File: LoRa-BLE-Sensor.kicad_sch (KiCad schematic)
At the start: 123 parts, among them J1 SHF-105-01-X-D-SM, J10 Battery_with_NTC, J2 Conn_01x02_Socket, J3 Battery_Cell, J4 Conn_01x06_Socket, J5 Screw_Terminal_01x06, J6 Screw_Terminal_01x06, J7 Screw_Terminal_01x04, J8 Conn_01x04_Pin, J9 Conn_01x04_Pin, Q1 DMN67D7L, Q10 SQ2389ES, Q11 SQ2389ES, Q12 DMN62D0UDW-7, Q13 DMN62D0UDW-7, Q2 DMN67D7L, Q3 DMN67D7L, Q4 DMN67D7L, Q5 DMN67D7L, Q6 DMN67D7L, Q7 DMN67D7L, Q8 DMN67D7L, Q9 SQ2389ES, SW1 SW_Push, SW2 SW_Push, SW3 SW_Push, U1 RAK4630, U2 NPM1300-QEAA-R, U3 TLV61046ADBVR, U4 TLV61046ADBVR, U5 TLV61046ADBVR

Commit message: rearranged board down to 60mm
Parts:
- J3: footprint User_Connectors:18650_CLIP_PROTECTED -> Connector_JST:JST_PH_B2B-PH-SM4-TB_1x02-1MP_P2.00mm_Vertical
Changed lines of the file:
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@@
 			)
 		)
-		(property "Footprint" "User_Connectors:18650_CLIP_PROTECTED"
+		(property "Footprint" "Connector_JST:JST_PH_B2B-PH-SM4-TB_1x02-1MP_P2.00mm_Vertical"
 			(at 196.85 22.606 90)
 			(effects

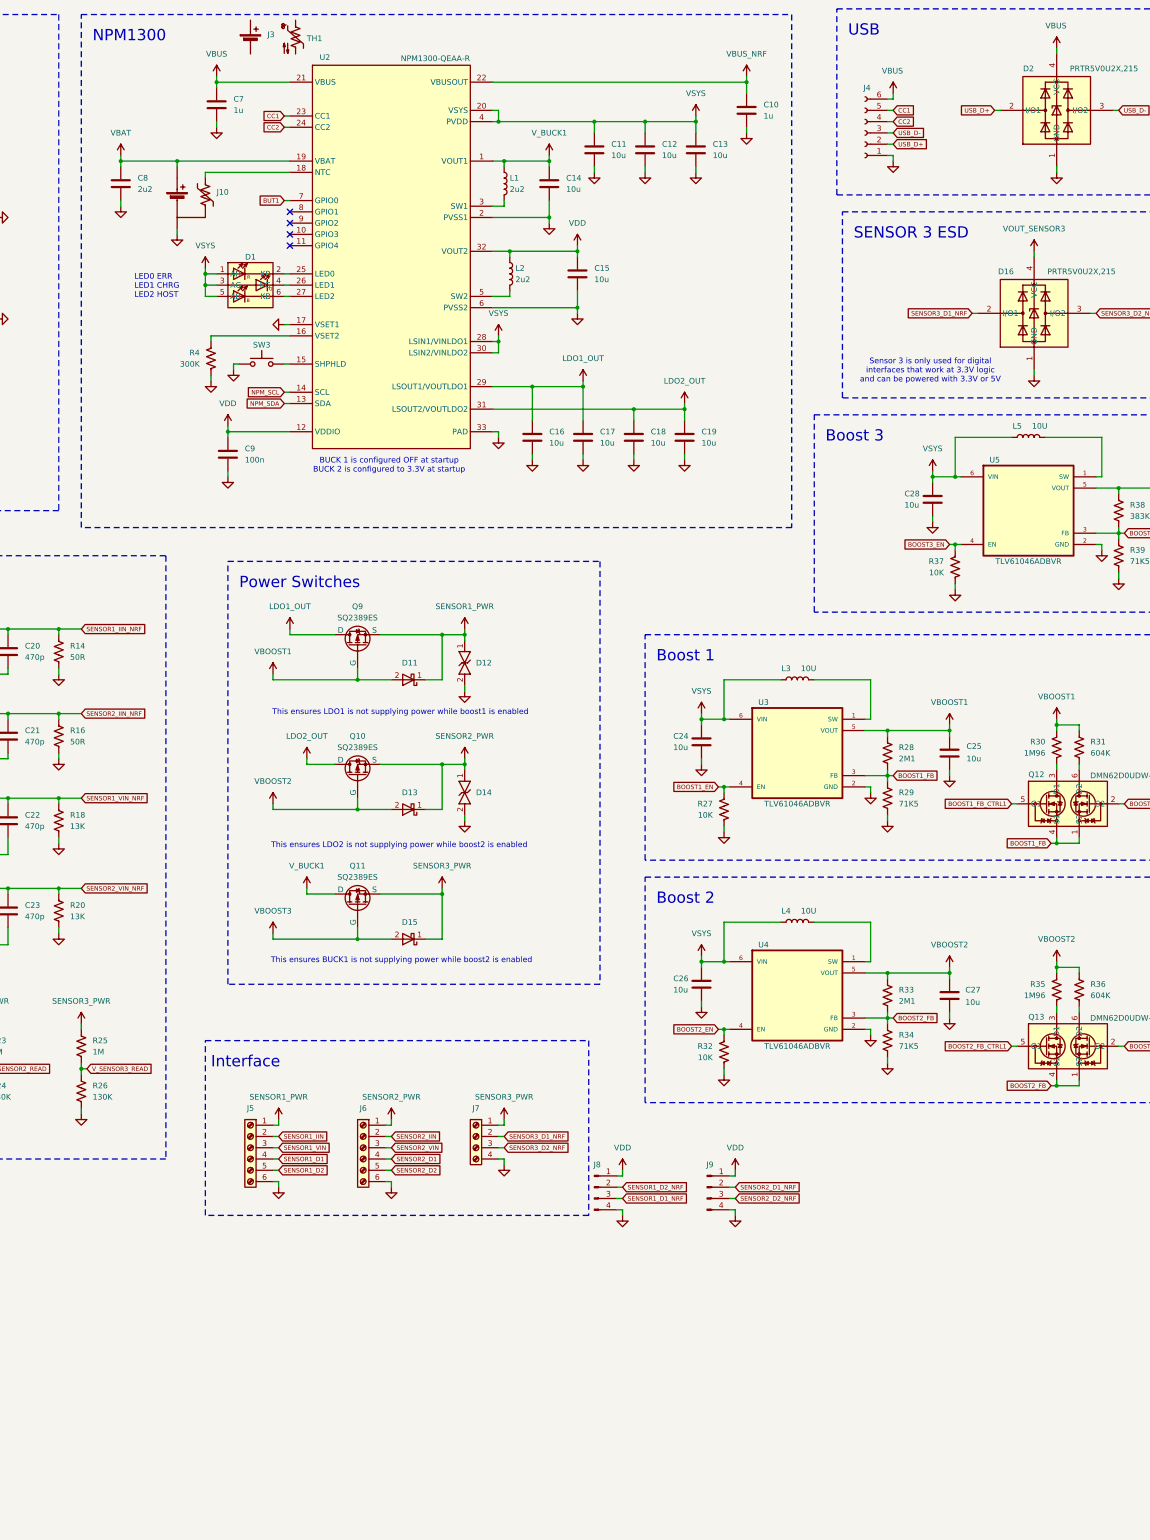
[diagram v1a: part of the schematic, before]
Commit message: external battery design finished
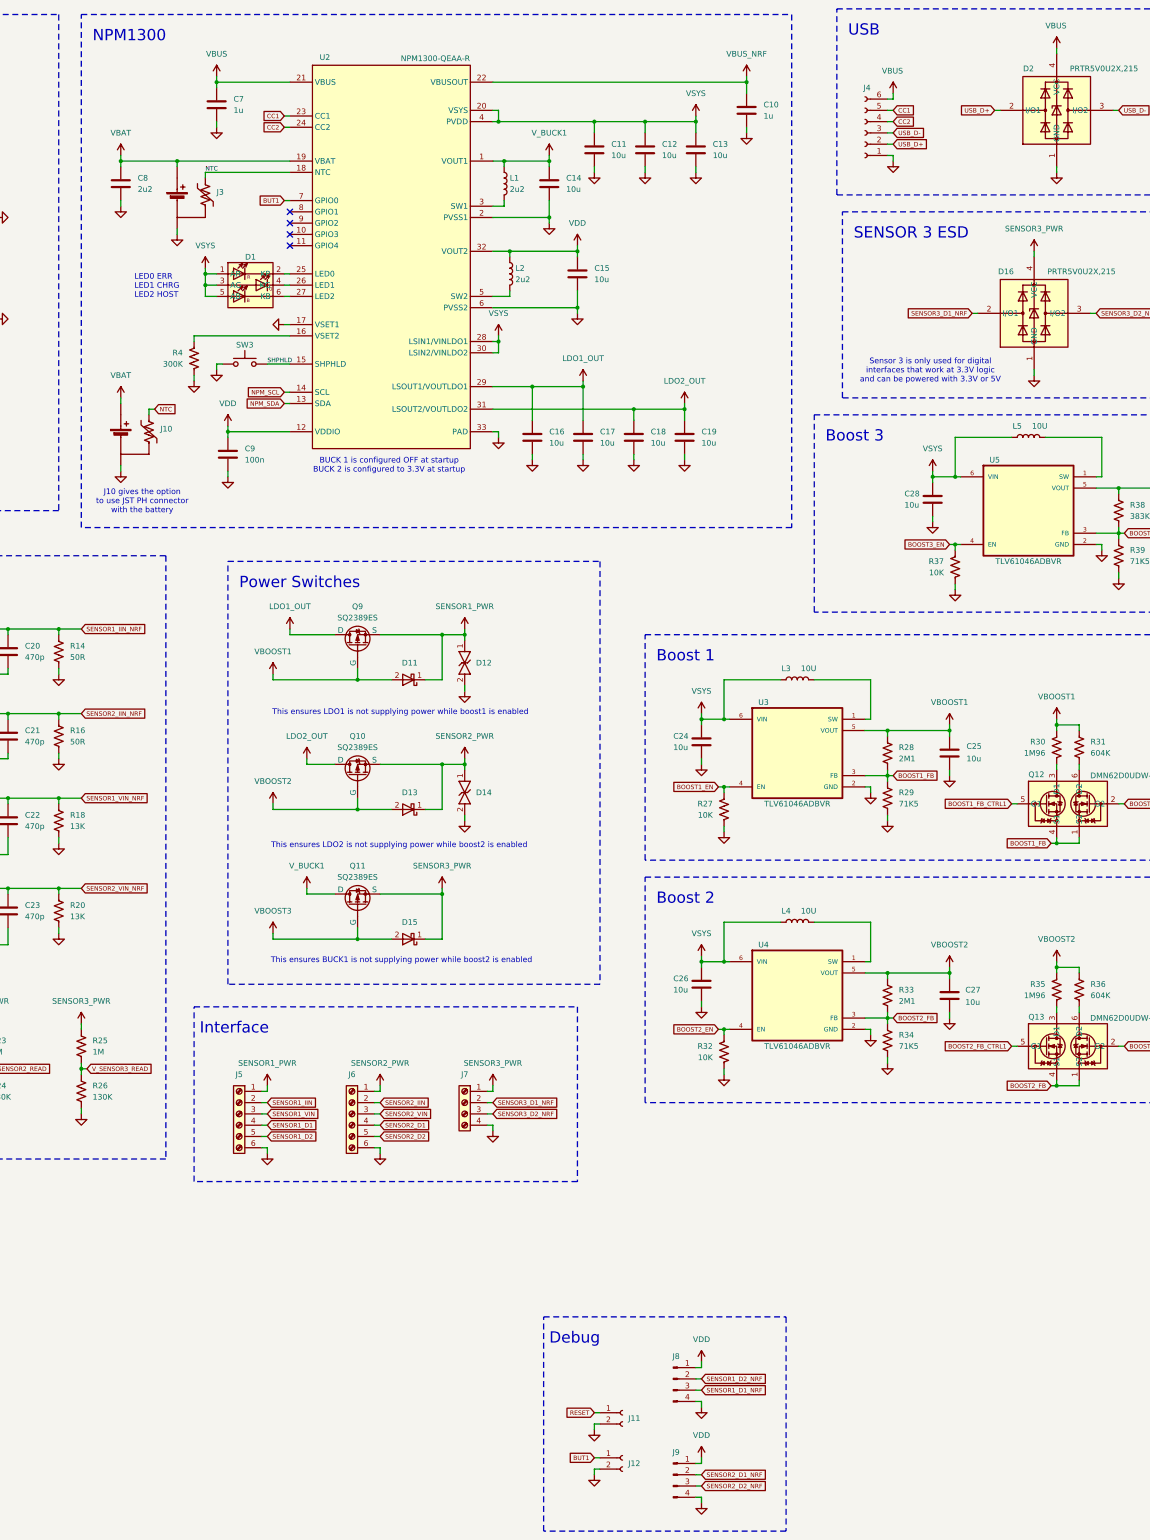
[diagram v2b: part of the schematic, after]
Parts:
- removed J3: Battery_Cell, Connector_JST:JST_PH_B2B-PH-SM4-TB_1x02-1MP_P2.00mm_Vertical, symbol Device:Battery_Cell
- removed TH1: 10K, Resistor_THT:R_Axial_DIN0204_L3.6mm_D1.6mm_P1.90mm_Vertical, symbol Device:Thermistor_NTC_US
- added J10: Battery_with_NTC, User_Connectors:JST_3PIN_PH_Vertical, symbol User_Connectors:Battery_with_NTC
- added J11, J12: Conn_01x02_Socket, User_Connectors:JST_SH_2-PIN_Vertical, symbol Connector:Conn_01x02_Socket
- renumbered J10 to J3
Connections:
- net VOUT_SENSOR3 is gone; now on net SENSOR3_PWR: D16.4 (VCC)
- net BUT1: now also J12.1 (Pin_1)
- net GND: now also J3.1 (-), J10.1 (-), J11.2 (Pin_2), J12.2 (Pin_2); no longer J3.3 (-)
- net RESET: now also J11.1 (Pin_1)
- net VBAT: now also J3.3 (+), J10.3 (+); no longer J3.1 (+)
- net SHPHLD: now reaches SW3.2, U2.15 (SHPHLD)
- net NTC: now reaches J3.2 (NTC), U2.18 (NTC)
- net NTC: now also J10.2 (NTC)
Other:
- note added: "Debug"
- note added: "J10 gives the option to use JST PH connector with the battery"
- moved on the sheet: J5, J6, J7, J8, J9, R4, SW3
